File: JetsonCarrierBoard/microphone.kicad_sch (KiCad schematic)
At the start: 0 parts

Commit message: Saved previously detailed changes
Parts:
- added C? (x2): (no value), symbol Device:C
- added R?: (no value), symbol Device:R
- added U? (x2): (no value), symbol I2S_MEMS_Microphone:ICS-43434
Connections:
- new net: U?.1 (WS), U?.1 (WS)
- new net: U?.4 (SCK), U?.4 (SCK)
- new net: R?.1, U?.6 (SD), U?.6 (SD)
- new net +1V8: C?.1, C?.1, U?.2 (LR), U?.5 (VDD), U?.5 (VDD)
- new net GND: C?.2, C?.2, R?.2, U?.2 (LR), U?.3 (GND), U?.3 (GND)
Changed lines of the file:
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@@
 (kicad_sch (version 20211123) (generator eeschema)
   (paper "A4")
+  (junction (at 167.64 92.71) (diameter 0) (color 0 0 0 0)
+  )
+  (junction (at 167.64 116.84) (diameter 0) (color 0 0 0 0)
+  )
+  (junction (at 125.73 116.84) (diameter 0) (color 0 0 0 0)
+  )
+  (junction (at 125.73 92.71) (diameter 0) (color 0 0 0 0)
+  )
+  (junction (at 177.8 105.41) (diameter 0) (color 0 0 0 0)
+  )
+  (junction (at 146.05 116.84) (diameter 0) (color 0 0 0 0)
+  )
+  (junction (at 146.05 107.95) (diameter 0) (color 0 0 0 0)
+  )
+  (junction (at 115.57 105.41) (diameter 0) (color 0 0 0 0)
+  )
+  (wire (pts (xy 135.89 107.95) (xy 146.05 107.95))
+    (stroke (width 0) (type default) (color 0 0 0 0))
+  )
+  (wire (pts (xy 125.73 116.84) (xy 125.73 118.11))
+    (stroke (width 0) (type default) (color 0 0 0 0))
+  )
+  (wire (pts (xy 177.8 92.71) (xy 167.64 92.71))
+    (stroke (width 0) (type default) (color 0 0 0 0))
+  )
+  (wire (pts (xy 135.89 102.87) (xy 157.48 102.87))
+    (stroke (width 0) (type default) (color 0 0 0 0))
+  )
+  (wire (pts (xy 125.73 116.84) (xy 146.05 116.84))
+    (stroke (width 0) (type default) (color 0 0 0 0))
+  )
+  (wire (pts (xy 177.8 116.84) (xy 167.64 116.84))
+    (stroke (width 0) (type default) (color 0 0 0 0))
+  )
+  (wire (pts (xy 115.57 105.41) (xy 115.57 116.84))
+    (stroke (width 0) (type default) (color 0 0 0 0))
+  )
+  (wire (pts (xy 125.73 90.17) (xy 125.73 92.71))
+    (stroke (width 0) (type default) (color 0 0 0 0))
+  )
+  (wire (pts (xy 167.64 90.17) (xy 167.64 92.71))
+    (stroke (width 0) (type default) (color 0 0 0 0))
+  )
+  (wire (pts (xy 125.73 92.71) (xy 125.73 95.25))
+    (stroke (width 0) (type default) (color 0 0 0 0))
+  )
+  (wire (pts (xy 115.57 100.33) (xy 115.57 105.41))
+    (stroke (width 0) (type default) (color 0 0 0 0))
+  )
+  (wire (pts (xy 177.8 105.41) (xy 177.8 92.71))
+    (stroke (width 0) (type default) (color 0 0 0 0))
+  )
+  (wire (pts (xy 177.8 115.57) (xy 177.8 116.84))
+    (stroke (width 0) (type default) (color 0 0 0 0))
+  )
+  (wire (pts (xy 167.64 115.57) (xy 167.64 116.84))
+    (stroke (width 0) (type default) (color 0 0 0 0))
+  )
+  (wire (pts (xy 115.57 116.84) (xy 125.73 116.84))
+    (stroke (width 0) (type default) (color 0 0 0 0))
+  )
+  (wire (pts (xy 167.64 92.71) (xy 167.64 95.25))
+    (stroke (width 0) (type default) (color 0 0 0 0))
+  )
+  (wire (pts (xy 146.05 107.95) (xy 157.48 107.95))
+    (stroke (width 0) (type default) (color 0 0 0 0))
+  )
+  (wire (pts (xy 177.8 105.41) (xy 177.8 107.95))
+    (stroke (width 0) (type default) (color 0 0 0 0))
+  )
+  (wire (pts (xy 167.64 116.84) (xy 167.64 118.11))
+    (stroke (width 0) (type default) (color 0 0 0 0))
+  )
+  (wire (pts (xy 115.57 92.71) (xy 125.73 92.71))
+    (stroke (width 0) (type default) (color 0 0 0 0))
+  )
+  (wire (pts (xy 146.05 107.95) (xy 146.05 109.22))
+    (stroke (width 0) (type default) (color 0 0 0 0))
+  )
+  (wire (pts (xy 146.05 116.84) (xy 167.64 116.84))
+    (stroke (width 0) (type default) (color 0 0 0 0))
+  )
+  (wire (pts (xy 125.73 115.57) (xy 125.73 116.84))
+    (stroke (width 0) (type default) (color 0 0 0 0))
+  )
+  (wire (pts (xy 135.89 105.41) (xy 157.48 105.41))
+    (stroke (width 0) (type default) (color 0 0 0 0))
+  )
+  (symbol (lib_id "I2S_MEMS_Microphone:ICS-43434") (at 125.73 105.41 0) (unit 1)
+    (in_bom yes) (on_board yes) (fields_autoplaced)
+    (property "Reference" "U?" (id 0) (at 127.7494 94.141 0)
+      (effects (font (size 1.27 1.27)) (justify left))
+    )
+    (property "Value" "" (id 1) (at 127.7494 96.6779 0)
+      (effects (font (size 1.27 1.27)) (justify left))
+    )
+    (property "Footprint" "" (id 2) (at 125.73 105.41 0)
+      (effects (font (size 1.27 1.27)) hide)
+    )
+    (property "Datasheet" "" (id 3) (at 125.73 105.41 0)
+      (effects (font (size 1.27 1.27)) hide)
+    )
+    (pin "1")
+    (pin "2")
+    (pin "3")
+    (pin "4")
+    (pin "5")
+    (pin "6")
+  )
+  (symbol (lib_id "power:+1V8") (at 125.73 90.17 0) (unit 1)
+    (in_bom yes) (on_board yes) (fields_autoplaced)
+    (property "Reference" "#PWR?" (id 0) (at 125.73 93.98 0)
+      (effects (font (size 1.27 1.27)) hide)
+    )
+    (property "Value" "" (id 1) (at 125.73 86.5942 0))
+    (property "Footprint" "" (id 2) (at 125.73 90.17 0)
+      (effects (font (size 1.27 1.27)) hide)
+    )
+    (property "Datasheet" "" (id 3) (at 125.73 90.17 0)
+      (effects (font (size 1.27 1.27)) hide)
+    )
+    (pin "1")
+  )
+  (symbol (lib_id "Device:C") (at 177.8 111.76 0) (unit 1)
+    (in_bom yes) (on_board yes)
+    (property "Reference" "C?" (id 0) (at 181.61 110.49 0)
+      (effects (font (size 1.27 1.27)) (justify left))
+    )
+    (property "Value" "" (id 1) (at 181.61 113.03 0)
+      (effects (font (size 1.27 1.27)) (justify left))
+    )
+    (property "Footprint" "" (id 2) (at 178.7652 115.57 0)
+      (effects (font (size 1.27 1.27)) hide)
+    )
+    (property "Datasheet" "~" (id 3) (at 177.8 111.76 0)
+      (effects (font (size 1.27 1.27)) hide)
+    )
+    (pin "1")
+    (pin "2")
+  )
+  (symbol (lib_id "power:+1V8") (at 167.64 90.17 0) (unit 1)
+    (in_bom yes) (on_board yes) (fields_autoplaced)
+    (property "Reference" "#PWR?" (id 0) (at 167.64 93.98 0)
+      (effects (font (size 1.27 1.27)) hide)
+    )
+    (property "Value" "" (id 1) (at 167.64 86.5942 0))
+    (property "Footprint" "" (id 2) (at 167.64 90.17 0)
+      (effects (font (size 1.27 1.27)) hide)
+    )
+    (property "Datasheet" "" (id 3) (at 167.64 90.17 0)
+      (effects (font (size 1.27 1.27)) hide)
+    )
+    (pin "1")
+  )
+  (symbol (lib_id "I2S_MEMS_Microphone:ICS-43434") (at 167.64 105.41 0) (mirror y) (unit 1)
+    (in_bom yes) (on_board yes)
+    (property "Reference" "U?" (id 0) (at 162.56 93.98 0))
+    (property "Value" "" (id 1) (at 158.75 96.5169 0))
+    (property "Footprint" "" (id 2) (at 167.64 105.41 0)
+      (effects (font (size 1.27 1.27)) hide)
+    )
+    (property "Datasheet" "" (id 3) (at 167.64 105.41 0)
+      (effects (font (size 1.27 1.27)) hide)
+    )
+    (pin "1")
+    (pin "2")
+    (pin "3")
+    (pin "4")
+    (pin "5")
+    (pin "6")
+  )
+  (symbol (lib_id "power:GND") (at 167.64 118.11 0) (unit 1)
+    (in_bom yes) (on_board yes) (fields_autoplaced)
+    (property "Reference" "#PWR?" (id 0) (at 167.64 124.46 0)
+      (effects (font (size 1.27 1.27)) hide)
+    )
+    (property "Value" "" (id 1) (at 167.64 122.5534 0))
+    (property "Footprint" "" (id 2) (at 167.64 118.11 0)
+      (effects (font (size 1.27 1.27)) hide)
+    )
+    (property "Datasheet" "" (id 3) (at 167.64 118.11 0)
+      (effects (font (size 1.27 1.27)) hide)
+    )
+    (pin "1")
+  )
+  (symbol (lib_id "Device:C") (at 115.57 96.52 0) (unit 1)
+    (in_bom yes) (on_board yes)
+    (property "Reference" "C?" (id 0) (at 110.49 95.25 0)
+      (effects (font (size 1.27 1.27)) (justify left))
+    )
+    (property "Value" "" (id 1) (at 107.95 97.79 0)
+      (effects (font (size 1.27 1.27)) (justify left))
+    )
+    (property "Footprint" "" (id 2) (at 116.5352 100.33 0)
+      (effects (font (size 1.27 1.27)) hide)
+    )
+    (property "Datasheet" "~" (id 3) (at 115.57 96.52 0)
+      (effects (font (size 1.27 1.27)) hide)
+    )
+    (pin "1")
+    (pin "2")
+  )
+  (symbol (lib_id "Device:R") (at 146.05 113.03 0) (unit 1)
+    (in_bom yes) (on_board yes) (fields_autoplaced)
+    (property "Reference" "R?" (id 0) (at 147.828 112.1953 0)
+      (effects (font (size 1.27 1.27)) (justify left))
+    )
+    (property "Value" "" (id 1) (at 147.828 114.7322 0)
+      (effects (font (size 1.27 1.27)) (justify left))
+    )
+    (property "Footprint" "" (id 2) (at 144.272 113.03 90)
+      (effects (font (size 1.27 1.27)) hide)
+    )
+    (property "Datasheet" "~" (id 3) (at 146.05 113.03 0)
+      (effects (font (size 1.27 1.27)) hide)
+    )
+    (pin "1")
+    (pin "2")
+  )
+  (symbol (lib_id "power:GND") (at 125.73 118.11 0) (unit 1)
+    (in_bom yes) (on_board yes) (fields_autoplaced)
+    (property "Reference" "#PWR?" (id 0) (at 125.73 124.46 0)
+      (effects (font (size 1.27 1.27)) hide)
+    )
+    (property "Value" "" (id 1) (at 125.73 122.5534 0))
+    (property "Footprint" "" (id 2) (at 125.73 118.11 0)
+      (effects (font (size 1.27 1.27)) hide)
+    )
+    (property "Datasheet" "" (id 3) (at 125.73 118.11 0)
+      (effects (font (size 1.27 1.27)) hide)
+    )
+    (pin "1")
+  )
 )

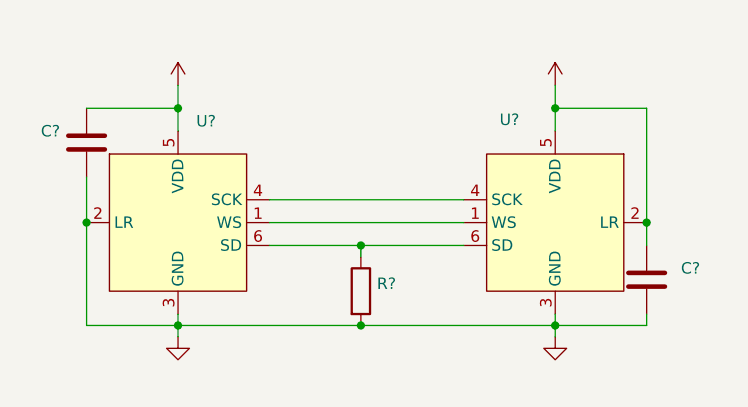
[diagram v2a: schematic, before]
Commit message: Added all USB-C components and started M.2 WiFi
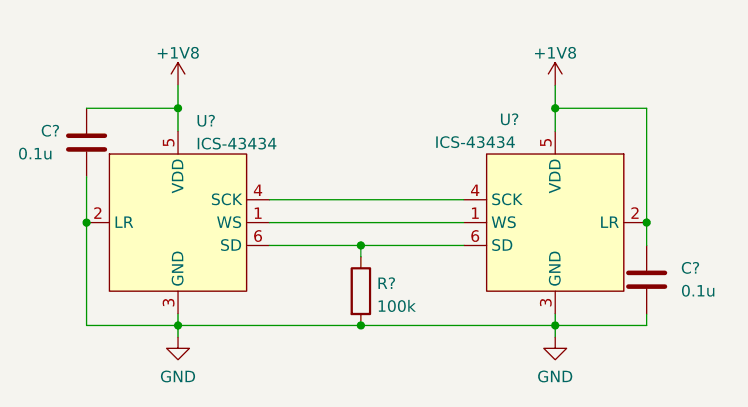
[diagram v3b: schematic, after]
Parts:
- C? (x2): value (none) -> 0.1u
- R?: value (none) -> 100k
- U? (x2): value (none) -> ICS-43434
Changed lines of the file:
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@@
       (effects (font (size 1.27 1.27)) (justify left))
     )
-    (property "Value" "" (id 1) (at 127.7494 96.6779 0)
+    (property "Value" "ICS-43434" (id 1) (at 127.7494 96.6779 0)
       (effects (font (size 1.27 1.27)) (justify left))
     )
@@
       (effects (font (size 1.27 1.27)) hide)
     )
-    (property "Value" "" (id 1) (at 125.73 86.5942 0))
+    (property "Value" "+1V8" (id 1) (at 125.73 86.5942 0))
     (property "Footprint" "" (id 2) (at 125.73 90.17 0)
       (effects (font (size 1.27 1.27)) hide)
@@
       (effects (font (size 1.27 1.27)) (justify left))
     )
-    (property "Value" "" (id 1) (at 181.61 113.03 0)
+    (property "Value" "0.1u" (id 1) (at 181.61 113.03 0)
       (effects (font (size 1.27 1.27)) (justify left))
     )
@@
       (effects (font (size 1.27 1.27)) hide)
     )
-    (property "Value" "" (id 1) (at 167.64 86.5942 0))
+    (property "Value" "+1V8" (id 1) (at 167.64 86.5942 0))
     (property "Footprint" "" (id 2) (at 167.64 90.17 0)
       (effects (font (size 1.27 1.27)) hide)
@@
     (in_bom yes) (on_board yes)
     (property "Reference" "U?" (id 0) (at 162.56 93.98 0))
-    (property "Value" "" (id 1) (at 158.75 96.5169 0))
+    (property "Value" "ICS-43434" (id 1) (at 158.75 96.5169 0))
     (property "Footprint" "" (id 2) (at 167.64 105.41 0)
       (effects (font (size 1.27 1.27)) hide)
@@
       (effects (font (size 1.27 1.27)) hide)
     )
-    (property "Value" "" (id 1) (at 167.64 122.5534 0))
+    (property "Value" "GND" (id 1) (at 167.64 122.5534 0))
     (property "Footprint" "" (id 2) (at 167.64 118.11 0)
       (effects (font (size 1.27 1.27)) hide)
@@
       (effects (font (size 1.27 1.27)) (justify left))
     )
-    (property "Value" "" (id 1) (at 107.95 97.79 0)
+    (property "Value" "0.1u" (id 1) (at 107.95 97.79 0)
       (effects (font (size 1.27 1.27)) (justify left))
     )
@@
       (effects (font (size 1.27 1.27)) (justify left))
     )
-    (property "Value" "" (id 1) (at 147.828 114.7322 0)
+    (property "Value" "100k" (id 1) (at 147.828 114.7322 0)
       (effects (font (size 1.27 1.27)) (justify left))
     )
@@
       (effects (font (size 1.27 1.27)) hide)
     )
-    (property "Value" "" (id 1) (at 125.73 122.5534 0))
+    (property "Value" "GND" (id 1) (at 125.73 122.5534 0))
     (property "Footprint" "" (id 2) (at 125.73 118.11 0)
       (effects (font (size 1.27 1.27)) hide)

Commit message: Small changes
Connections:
- net MIC_WS: now reaches U?.1 (WS), U?.1 (WS)
- net MIC_SCK: now reaches U?.4 (SCK), U?.4 (SCK)
- net MIC_SD: now reaches R?.1, U?.6 (SD), U?.6 (SD)
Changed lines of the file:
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@@
 (kicad_sch (version 20211123) (generator eeschema)
   (paper "A4")
+  (junction (at 142.24 102.87) (diameter 0) (color 0 0 0 0)
+  )
   (junction (at 167.64 92.71) (diameter 0) (color 0 0 0 0)
   )
   (junction (at 167.64 116.84) (diameter 0) (color 0 0 0 0)
+  )
+  (junction (at 146.05 105.41) (diameter 0) (color 0 0 0 0)
   )
   (junction (at 125.73 116.84) (diameter 0) (color 0 0 0 0)
@@
   )
   (junction (at 177.8 105.41) (diameter 0) (color 0 0 0 0)
+  )
+  (junction (at 149.86 107.95) (diameter 0) (color 0 0 0 0)
   )
   (junction (at 146.05 116.84) (diameter 0) (color 0 0 0 0)
@@
     (stroke (width 0) (type default) (color 0 0 0 0))
   )
-  (wire (pts (xy 135.89 102.87) (xy 157.48 102.87))
+  (wire (pts (xy 135.89 102.87) (xy 142.24 102.87))
     (stroke (width 0) (type default) (color 0 0 0 0))
   )
@@
     (stroke (width 0) (type default) (color 0 0 0 0))
   )
+  (wire (pts (xy 146.05 105.41) (xy 157.48 105.41))
+    (stroke (width 0) (type default) (color 0 0 0 0))
+  )
   (wire (pts (xy 115.57 100.33) (xy 115.57 105.41))
     (stroke (width 0) (type default) (color 0 0 0 0))
@@
     (stroke (width 0) (type default) (color 0 0 0 0))
   )
-  (wire (pts (xy 146.05 107.95) (xy 157.48 107.95))
+  (wire (pts (xy 149.86 107.95) (xy 157.48 107.95))
+    (stroke (width 0) (type default) (color 0 0 0 0))
+  )
+  (wire (pts (xy 146.05 107.95) (xy 149.86 107.95))
     (stroke (width 0) (type default) (color 0 0 0 0))
   )
@@
     (stroke (width 0) (type default) (color 0 0 0 0))
   )
+  (wire (pts (xy 142.24 95.25) (xy 142.24 102.87))
+    (stroke (width 0) (type default) (color 0 0 0 0))
+  )
+  (wire (pts (xy 149.86 95.25) (xy 149.86 107.95))
+    (stroke (width 0) (type default) (color 0 0 0 0))
+  )
   (wire (pts (xy 146.05 116.84) (xy 167.64 116.84))
+    (stroke (width 0) (type default) (color 0 0 0 0))
+  )
+  (wire (pts (xy 146.05 95.25) (xy 146.05 105.41))
+    (stroke (width 0) (type default) (color 0 0 0 0))
+  )
+  (wire (pts (xy 142.24 102.87) (xy 157.48 102.87))
     (stroke (width 0) (type default) (color 0 0 0 0))
   )
@@
     (stroke (width 0) (type default) (color 0 0 0 0))
   )
-  (wire (pts (xy 135.89 105.41) (xy 157.48 105.41))
+  (wire (pts (xy 135.89 105.41) (xy 146.05 105.41))
     (stroke (width 0) (type default) (color 0 0 0 0))
   )
+  (global_label "MIC_SD" (shape input) (at 149.86 95.25 90) (fields_autoplaced)
+    (effects (font (size 1.27 1.27)) (justify left))
+    (property "Intersheet References" "${INTERSHEET_REFS}" (id 0) (at 149.7806 86.0636 90)
+      (effects (font (size 1.27 1.27)) (justify left) hide)
+    )
+  )
+  (global_label "MIC_WS" (shape output) (at 146.05 95.25 90) (fields_autoplaced)
+    (effects (font (size 1.27 1.27)) (justify left))
+    (property "Intersheet References" "${INTERSHEET_REFS}" (id 0) (at 145.9706 85.8821 90)
+      (effects (font (size 1.27 1.27)) (justify left) hide)
+    )
+  )
+  (global_label "MIC_SCK" (shape input) (at 142.24 95.25 90) (fields_autoplaced)
+    (effects (font (size 1.27 1.27)) (justify left))
+    (property "Intersheet References" "${INTERSHEET_REFS}" (id 0) (at 142.1606 84.7936 90)
+      (effects (font (size 1.27 1.27)) (justify left) hide)
+    )
+  )
   (symbol (lib_id "I2S_MEMS_Microphone:ICS-43434") (at 125.73 105.41 0) (unit 1)
